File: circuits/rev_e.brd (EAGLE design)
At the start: 61 x 58 mm, 16 parts, among them X1 ENCODER_ANO

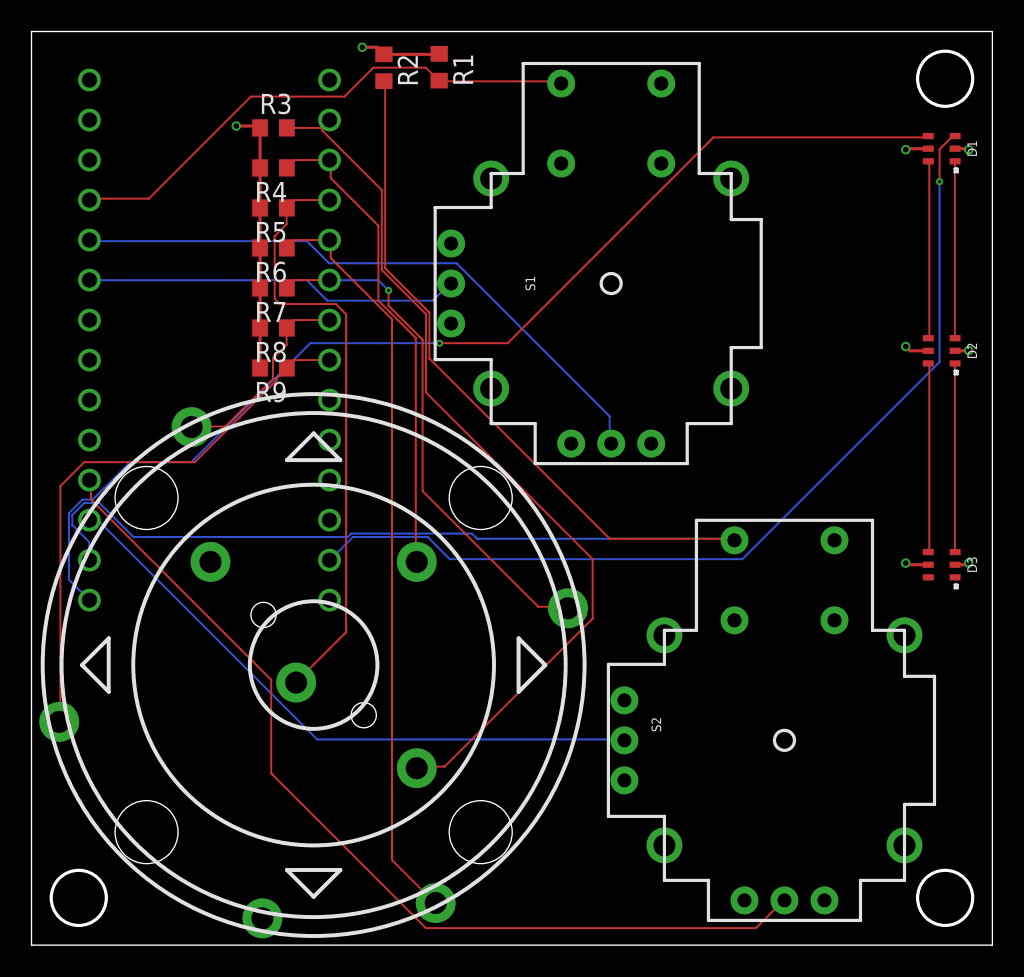
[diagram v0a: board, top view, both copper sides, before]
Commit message: Updated docs, also sent `rev_d` to production.
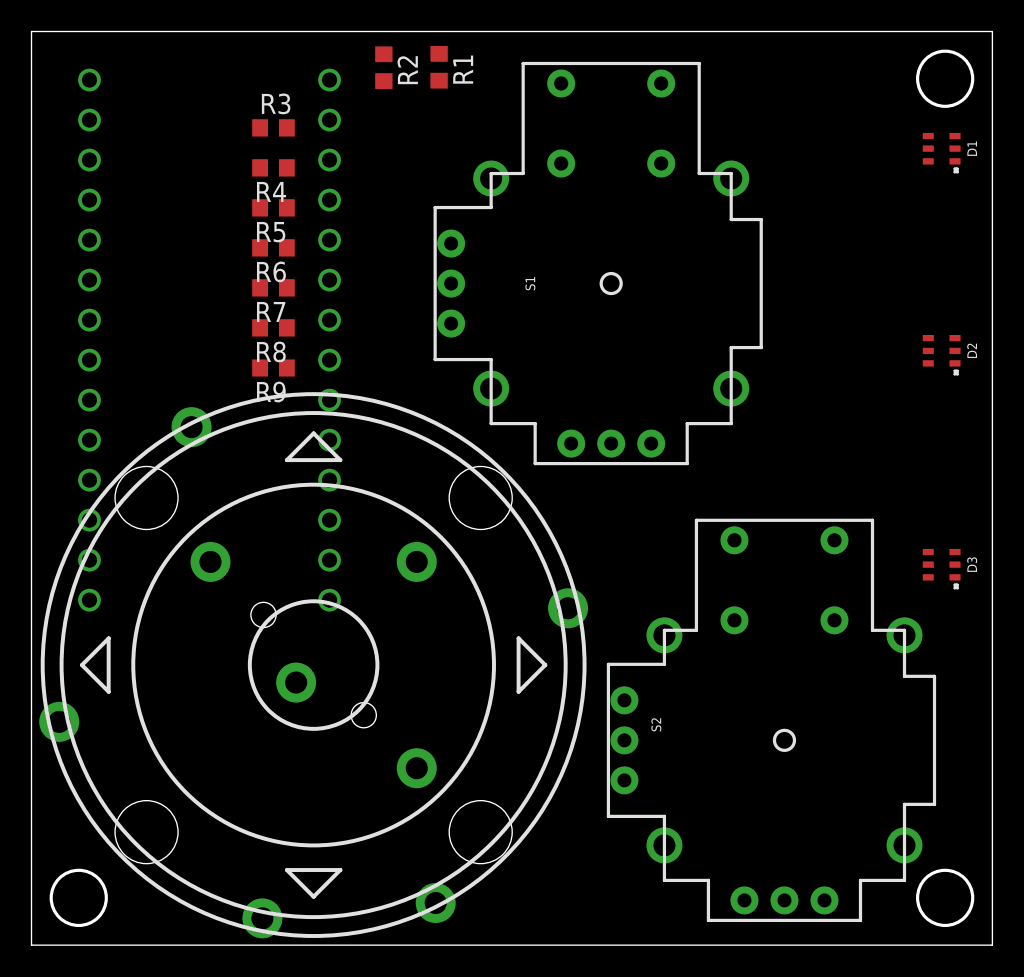
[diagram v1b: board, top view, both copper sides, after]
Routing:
- net +3V3: track 185.9 -> 0.00 mm, vias 5 -> 0
- net S2: track 89.9 -> 0.00 mm
- net N$12: track 70.5 -> 0.00 mm, vias 1 -> 0
- net HOR2: track 60.8 -> 0.00 mm
- net N$13: track 60.0 -> 0.00 mm, vias 1 -> 0
- net N$7: track 57.0 -> 0.00 mm
- net N$4: track 47.8 -> 0.00 mm
- net VERT2: track 39.7 -> 0.00 mm
- net HOR1: track 39.5 -> 0.00 mm
- net N$5: track 38.6 -> 0.00 mm
- net N$1: track 35.5 -> 0.00 mm
- net S1: track 33.8 -> 0.00 mm
- net N$3: track 32.9 -> 0.00 mm, vias 1 -> 0
- net N$6: track 30.7 -> 0.00 mm
- net VERT1: track 23.9 -> 0.00 mm
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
